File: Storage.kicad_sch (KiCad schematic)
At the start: 4 parts, among them J6 Micro_SD_Card_Det1, U9 Tudi AT24CM02-SSHD-T-TUDI

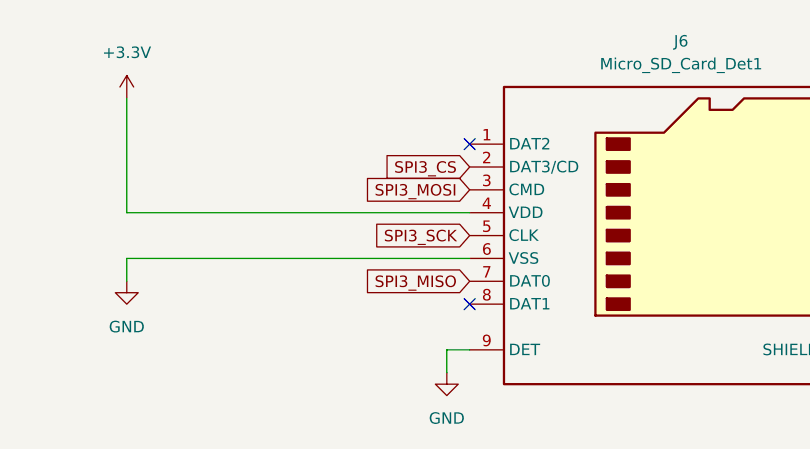
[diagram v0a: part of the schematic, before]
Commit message: add sd card reader
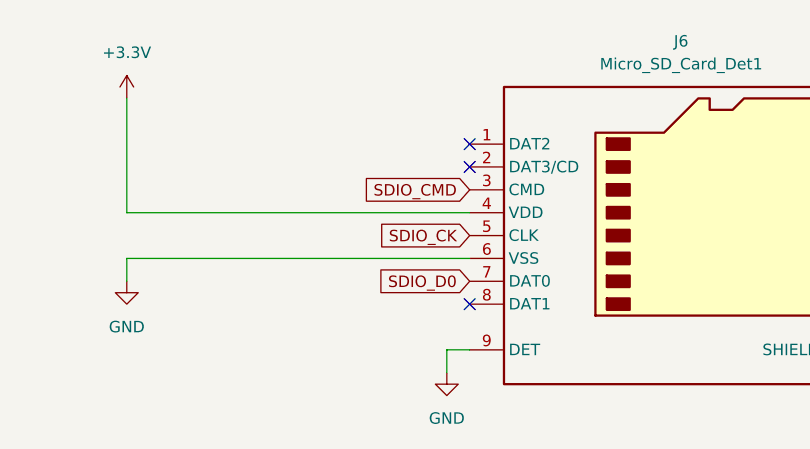
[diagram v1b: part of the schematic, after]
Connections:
- net SPI3_CS: no longer names the net of J6.2 (DAT3/CD)
- net SPI3_MISO renamed SDIO_D0
- net SPI3_MOSI renamed SDIO_CMD
- net SPI3_SCK renamed SDIO_CK
- no-connect marks 2 -> 3
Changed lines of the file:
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@@
+	)
+	(no_connect
+		(at 151.13 43.18)
 	)
 	(no_connect
@@
 		)
 	)
-	(global_label "SPI3_MISO"
+	(global_label "SDIO_D0"
 		(shape input)
 		(at 151.13 55.88 180)
@@
 		)
 		(property "Intersheetrefs" "${INTERSHEET_REFS}"
-			(at 138.2872 55.88 0)
+			(at 140.2829 55.88 0)
 			(effects
 				(font
@@
 		)
 	)
-	(global_label "SPI3_CS"
-		(shape input)
-		(at 151.13 43.18 180)
+	(global_label "SDIO_CK"
+		(shape input)
+		(at 151.13 50.8 180)
 		(fields_autoplaced yes)
 		(effects
@@
 		)
 		(property "Intersheetrefs" "${INTERSHEET_REFS}"
-			(at 140.4039 43.18 0)
+			(at 140.2224 50.8 0)
 			(effects
 				(font
@@
 		)
 	)
-	(global_label "SPI3_SCK"
-		(shape input)
-		(at 151.13 50.8 180)
-		(fields_autoplaced yes)
-		(effects
-			(font
-				(size 1.27 1.27)
-			)
-			(justify right)
-		)
-		(property "Intersheetrefs" "${INTERSHEET_REFS}"
-			(at 139.1339 50.8 0)
-			(effects
-				(font
-					(size 1.27 1.27)
-				)
-				(justify right)
-				(hide yes)
-			)
-		)
-	)
 	(global_label "I2C2_SDA"
 		(shape input)
@@
 		)
 	)
-	(global_label "SPI3_MOSI"
+	(global_label "SDIO_CMD"
 		(shape input)
 		(at 151.13 45.72 180)
@@
 		)
 		(property "Intersheetrefs" "${INTERSHEET_REFS}"
-			(at 138.2872 45.72 0)
-			(effects
-				(font
+			(at 138.771 45.72 0)
+			(effects
+				(font

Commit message: "Update KiRA Flight Computer schematic and PCB files"
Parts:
- J6: footprint (none) -> Connector_Card:microSD_HC_Hirose_DM3BT-DSF-PEJS
- R16, R17: footprint (none) -> Resistor_SMD:R_0603_1608Metric
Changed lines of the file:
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@@
 			)
 		)
-		(property "Footprint" ""
+		(property "Footprint" "Resistor_SMD:R_0603_1608Metric"
 			(at 70.612 43.18 90)
 			(effects
@@
 			)
 		)
-		(property "Footprint" ""
+		(property "Footprint" "Connector_Card:microSD_HC_Hirose_DM3BT-DSF-PEJS"
 			(at 226.06 33.02 0)
 			(effects
@@
 			)
 		)
-		(property "Footprint" ""
+		(property "Footprint" "Resistor_SMD:R_0603_1608Metric"
 			(at 60.452 43.18 90)
 			(effects

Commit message: Update PCB
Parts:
- J6: footprint Connector_Card:microSD_HC_Hirose_DM3BT-DSF-PEJS -> Connector_Card:microSD_HC_Hirose_DM3AT-SF-PEJM5
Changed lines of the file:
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@@
 			)
 		)
-		(property "Footprint" "Connector_Card:microSD_HC_Hirose_DM3BT-DSF-PEJS"
+		(property "Footprint" "Connector_Card:microSD_HC_Hirose_DM3AT-SF-PEJM5"
 			(at 226.06 33.02 0)
 			(effects
@@
 					(size 1.27 1.27)
 				)
-				(hide yes)
 			)
 		)
